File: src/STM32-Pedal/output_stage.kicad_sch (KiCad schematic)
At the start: 0 parts

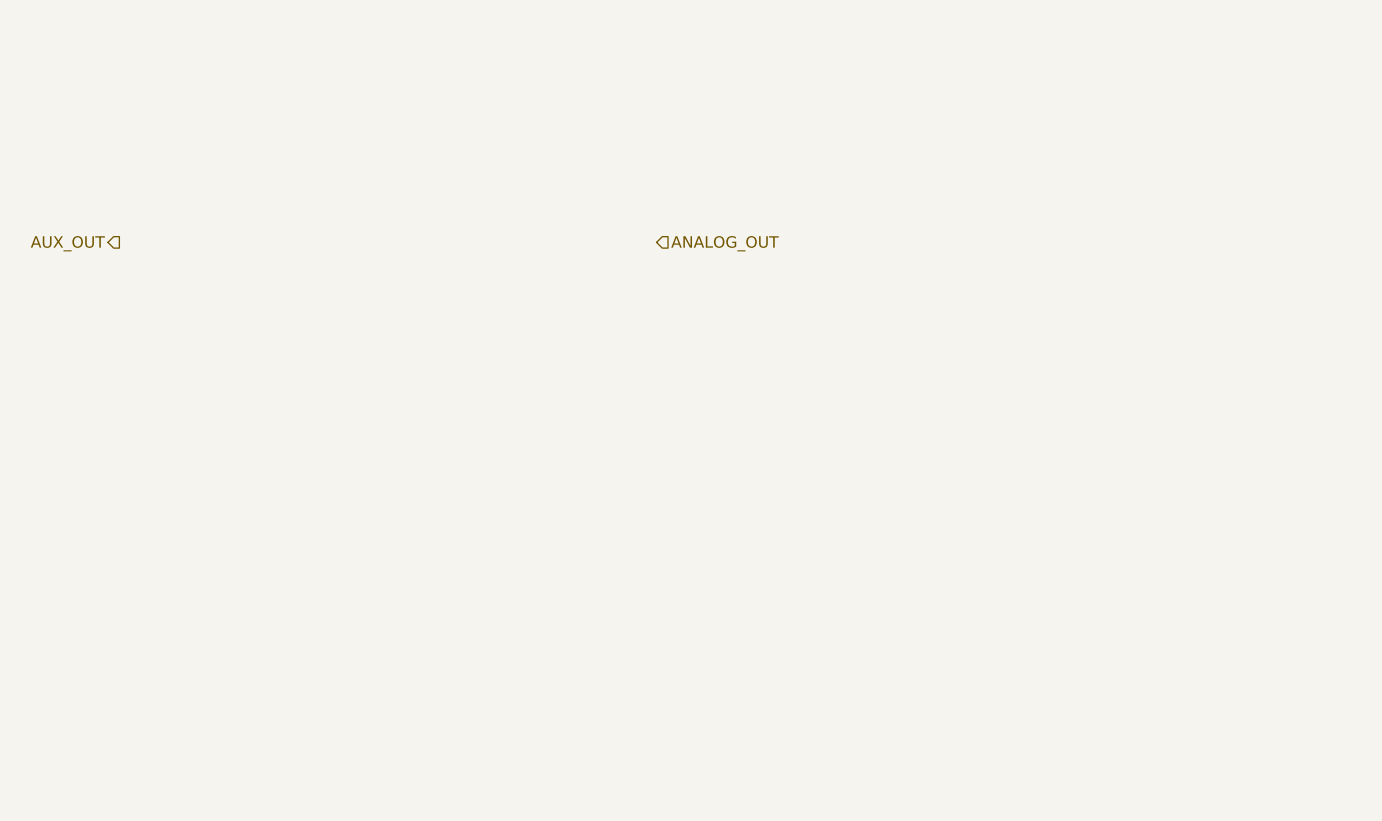
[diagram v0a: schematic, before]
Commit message: Schematic: bypass relay, cleaning up input stage
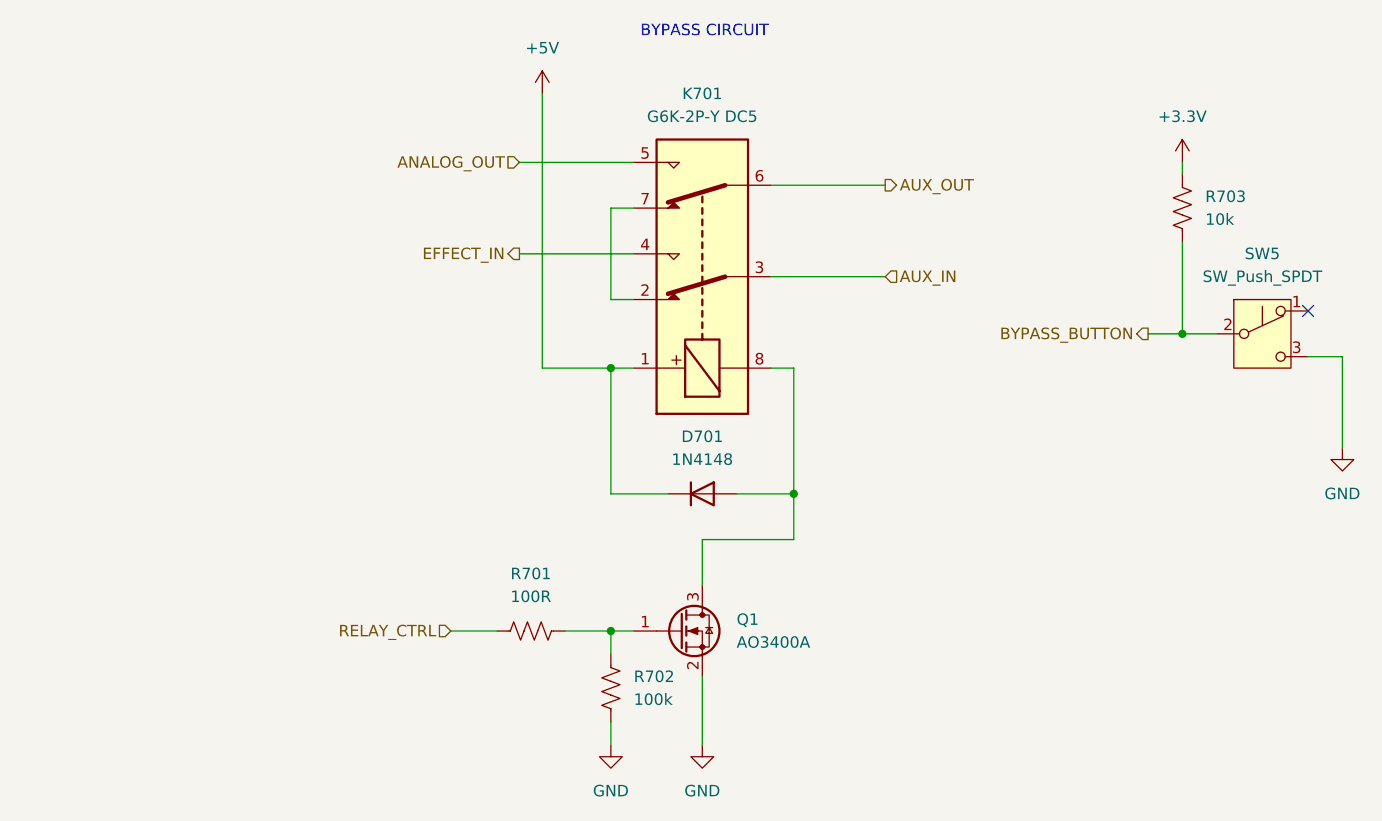
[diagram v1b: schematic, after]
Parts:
- added D701: 1N4148, Diode_THT:D_DO-35_SOD27_P7.62mm_Horizontal, symbol Diode:1N4148
- added K701: G6K-2P-Y DC5, Relay_THT:Relay_DPDT_Omron_G6K-2P-Y, symbol Relay:G6K-2
- added Q1: AO3400A, Package_TO_SOT_SMD:SOT-23, symbol Transistor_FET:AO3400A
- added R701: 100R, Resistor_SMD:R_0603_1608Metric_Pad0.98x0.95mm_HandSolder, symbol Device:R_US
- added R702: 100k, Resistor_SMD:R_0603_1608Metric_Pad0.98x0.95mm_HandSolder, symbol Device:R_US
- added R703: 10k, Resistor_SMD:R_0603_1608Metric_Pad0.98x0.95mm_HandSolder, symbol Device:R_US
- added SW5: SW_Push_SPDT, symbol Switch:SW_Push_SPDT
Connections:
- net ANALOG_OUT: now also K701.5
- net AUX_OUT: now also K701.6
- new net: Q1.1 (G), R701.2, R702.1
- new net: D701.2 (A), K701.8, Q1.3 (D)
- new net: K701.2, K701.7
- new net +3.3V: R703.1
- new net +5V: D701.1 (K), K701.1
- new net AUX_IN: K701.3
- new net BYPASS_BUTTON: R703.2, SW5.2 (B)
- new net EFFECT_IN: K701.4
- new net GND: Q1.2 (S), R702.2, SW5.3 (C)
- new net RELAY_CTRL: R701.1
- no-connect marks 0 -> 1
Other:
- note added: "BYPASS CIRCUIT"
